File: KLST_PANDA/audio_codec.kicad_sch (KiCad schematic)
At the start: 45 parts, among them J16 MIC_IN, J17 LINE_IN, J18 HEADPHONE_OUT, J19 LINE_OUT, U9 WM8904CGEFL/V

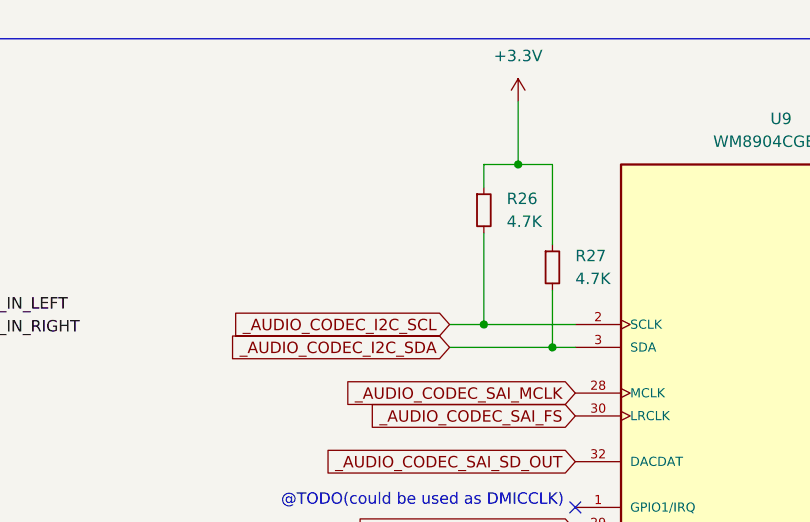
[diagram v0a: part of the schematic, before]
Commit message: changed I2C label, display can now be switched on and off
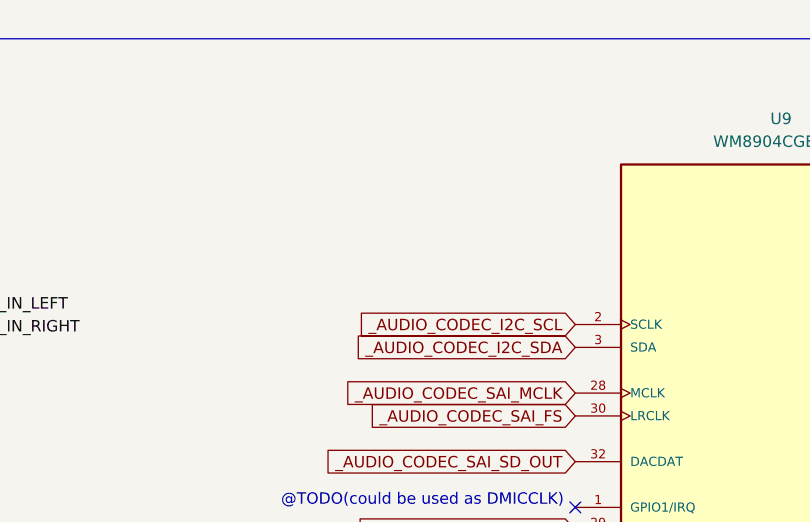
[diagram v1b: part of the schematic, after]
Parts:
- removed R26, R27: 4.7K, symbol Device:R_Small
- U9: footprint QFN40P400X400X80-33N -> WM8904CGEFL:QFN40P400X400X80-33N

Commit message: cleaned up
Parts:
- J18: value HEADPHONE_OUT -> HEADPHONE_OUT+MIC
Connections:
- net HEADPHONE_GND: no longer J18.S
- net MIC_IN_MONO: now reaches C16.2, FB1.1, J16.T
- net MIC_IN_MONO: now also J18.S
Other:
- note removed: "@TODO( consider merging microphone+headphone into a single CTIA/AHJ connector )"
- note removed: "@TODO(could be used as DMICCLK)"
- note removed: "@TODO(could be used as DMICDAT)"
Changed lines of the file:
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@@
   (junction (at 280.035 35.56) (diameter 0) (color 0 0 0 0)
   )
-  (junction (at 351.79 54.61) (diameter 0) (color 0 0 0 0)
-  )
-  (junction (at 331.47 54.61) (diameter 0) (color 0 0 0 0)
+  (junction (at 331.47 49.53) (diameter 0) (color 0 0 0 0)
   )
   (junction (at 82.55 41.91) (diameter 0) (color 0 0 0 0)
@@
   (junction (at 291.465 35.56) (diameter 0) (color 0 0 0 0)
   )
-  (junction (at 344.17 52.07) (diameter 0) (color 0 0 0 0)
+  (junction (at 344.17 46.99) (diameter 0) (color 0 0 0 0)
   )
   (junction (at 115.57 107.95) (diameter 0) (color 0 0 0 0)
@@
   )
   (junction (at 331.47 95.25) (diameter 0) (color 0 0 0 0)
+  )
+  (junction (at 50.165 44.45) (diameter 0) (color 0 0 0 0)
   )
   (junction (at 254.635 35.56) (diameter 0) (color 0 0 0 0)
@@
     (stroke (width 0) (type default))
   )
-  (wire (pts (xy 289.56 57.15) (xy 351.79 57.15))
+  (wire (pts (xy 289.56 52.07) (xy 356.87 52.07))
     (stroke (width 0) (type default))
   )
@@
     (stroke (width 0) (type default))
   )
-  (wire (pts (xy 349.25 49.53) (xy 356.87 49.53))
+  (wire (pts (xy 331.47 49.53) (xy 356.87 49.53))
     (stroke (width 0) (type default))
   )
@@
     (stroke (width 0) (type default))
   )
-  (wire (pts (xy 351.79 52.07) (xy 351.79 54.61))
-    (stroke (width 0) (type default))
-  )
   (wire (pts (xy 281.94 95.25) (xy 281.94 72.39))
     (stroke (width 0) (type default))
@@
     (stroke (width 0) (type default))
   )
-  (wire (pts (xy 331.47 54.61) (xy 331.47 78.74))
+  (wire (pts (xy 331.47 49.53) (xy 331.47 78.74))
     (stroke (width 0) (type default))
   )
@@
     (stroke (width 0) (type default))
   )
-  (wire (pts (xy 346.71 44.45) (xy 346.71 52.07))
+  (wire (pts (xy 346.71 44.45) (xy 346.71 46.99))
     (stroke (width 0) (type default))
   )
@@
     (stroke (width 0) (type default))
   )
-  (wire (pts (xy 351.79 57.15) (xy 351.79 54.61))
-    (stroke (width 0) (type default))
-  )
   (wire (pts (xy 99.06 101.6) (xy 97.79 101.6))
     (stroke (width 0) (type default))
@@
     (stroke (width 0) (type default))
   )
+  (wire (pts (xy 289.56 54.61) (xy 356.87 54.61))
+    (stroke (width 0) (type default))
+  )
   (wire (pts (xy 217.17 74.93) (xy 269.24 74.93))
     (stroke (width 0) (type default))
@@
     (stroke (width 0) (type default))
   )
-  (polyline (pts (xy 15.24 116.84) (xy 388.62 116.84))
-    (stroke (width 0) (type default))
-  )
   (wire (pts (xy 105.41 93.98) (xy 105.41 101.6))
     (stroke (width 0) (type default))
@@
     (stroke (width 0) (type default))
   )
-  (wire (pts (xy 344.17 52.07) (xy 344.17 78.74))
-    (stroke (width 0) (type default))
-  )
   (wire (pts (xy 127 87.63) (xy 121.92 87.63))
     (stroke (width 0) (type default))
@@
     (stroke (width 0) (type default))
   )
-  (wire (pts (xy 331.47 54.61) (xy 349.25 54.61))
-    (stroke (width 0) (type default))
-  )
-  (wire (pts (xy 38.1 44.45) (xy 60.96 44.45))
+  (wire (pts (xy 38.1 44.45) (xy 50.165 44.45))
     (stroke (width 0) (type default))
   )
@@
     (stroke (width 0) (type default))
   )
+  (wire (pts (xy 50.165 44.45) (xy 60.96 44.45))
+    (stroke (width 0) (type default))
+  )
   (wire (pts (xy 105.41 83.82) (xy 104.14 83.82))
     (stroke (width 0) (type default))
@@
     (stroke (width 0) (type default))
   )
-  (wire (pts (xy 344.17 52.07) (xy 346.71 52.07))
+  (wire (pts (xy 344.17 46.99) (xy 346.71 46.99))
     (stroke (width 0) (type default))
   )
@@
     (stroke (width 0) (type default))
   )
-  (wire (pts (xy 351.79 54.61) (xy 356.87 54.61))
-    (stroke (width 0) (type default))
-  )
   (wire (pts (xy 38.1 91.44) (xy 46.99 91.44))
     (stroke (width 0) (type default))
@@
     (stroke (width 0) (type default))
   )
-  (wire (pts (xy 349.25 49.53) (xy 349.25 54.61))
-    (stroke (width 0) (type default))
-  )
   (wire (pts (xy 289.56 62.23) (xy 318.77 62.23))
     (stroke (width 0) (type default))
@@
     (stroke (width 0) (type default))
   )
+  (wire (pts (xy 344.17 46.99) (xy 344.17 78.74))
+    (stroke (width 0) (type default))
+  )
   (wire (pts (xy 99.06 48.26) (xy 99.06 52.07))
     (stroke (width 0) (type default))
@@
     (stroke (width 0) (type default))
   )
-  (wire (pts (xy 289.56 54.61) (xy 331.47 54.61))
+  (wire (pts (xy 289.56 49.53) (xy 331.47 49.53))
     (stroke (width 0) (type default))
   )
@@
     (stroke (width 0) (type default))
   )
-  (polyline (pts (xy 15.24 116.84) (xy 15.24 15.24))
-    (stroke (width 0) (type default))
-  )
   (wire (pts (xy 220.98 22.225) (xy 220.98 31.75))
     (stroke (width 0) (type default))
   )
-  (wire (pts (xy 351.79 52.07) (xy 356.87 52.07))
+  (wire (pts (xy 50.165 26.67) (xy 50.165 44.45))
     (stroke (width 0) (type default))
   )
@@
     (stroke (width 0) (type default))
   )
-  (wire (pts (xy 289.56 52.07) (xy 344.17 52.07))
+  (wire (pts (xy 289.56 46.99) (xy 344.17 46.99))
     (stroke (width 0) (type default))
   )
@@
     (stroke (width 0) (type default))
   )
-  (polyline (pts (xy 388.62 15.24) (xy 388.62 116.84))
-    (stroke (width 0) (type default))
-  )
   (wire (pts (xy 86.36 107.95) (xy 115.57 107.95))
     (stroke (width 0) (type default))
@@
     (stroke (width 0) (type default))
   )
-  (polyline (pts (xy 15.24 15.24) (xy 388.62 15.24))
-    (stroke (width 0) (type default))
-  )
   (wire (pts (xy 254.635 22.225) (xy 254.635 25.4))
     (stroke (width 0) (type default))
@@
     (stroke (width 0) (type default))
   )
+  (rectangle (start 15.24 15.24) (end 396.24 119.38)
+    (stroke (width 0) (type default))
+    (fill (type none))
+  )
   (rectangle (start 250.825 24.13) (end 314.325 36.83)
     (stroke (width 0) (type default))
     (fill (type none))
+  )
+  (text_box "MIC_IN_MONO is connected to MIC_IN_LEFT and SLEEVE ( CTIA/AHJ )"
+    (at 360.68 27.305 0) (size 24.13 10.16)
+    (stroke (width 0) (type default))
+    (fill (type none))
+    (effects (font (size 1.27 1.27)) (justify left bottom))
   )
   (text "see datasheet Table 95, p177" (at 227.33 105.41 0)
@@
     (effects (font (size 1.27 1.27)) (justify left bottom))
   )
-  (text "@TODO(could be used as DMICDAT)" (at 157.48 74.93 0)
-    (effects (font (size 1.27 1.27)) (justify right bottom))
-  )
-  (text "@TODO( consider merging microphone+headphone into a single CTIA/AHJ connector )"
-    (at 332.74 43.18 0)
-    (effects (font (size 1.27 1.27)) (justify left bottom))
-  )
   (text "TANTALUM" (at 97.79 106.68 0)
     (effects (font (size 1.27 1.27)) (justify left bottom))
@@
   (text "6.3V" (at 246.38 101.6 0)
     (effects (font (size 1.27 1.27)) (justify left bottom))
-  )
-  (text "@TODO(could be used as DMICCLK)" (at 170.18 67.31 0)
-    (effects (font (size 1.27 1.27)) (justify right bottom))
   )
   (text "should be reasonably close to WM8904" (at 302.26 77.47 0)
@@
     (effects (font (size 1.27 1.27)) (justify right bottom))
   )
+  (label "MIC_IN_MONO" (at 289.56 54.61 0) (fields_autoplaced)
+    (effects (font (size 1.27 1.27)) (justify left bottom))
+  )
   (label "LINE_IN_LEFT" (at 171.45 82.55 180) (fields_autoplaced)
     (effects (font (size 1.27 1.27)) (justify right bottom))
   )
-  (label "HEADPHONE_GND" (at 289.56 57.15 0) (fields_autoplaced)
+  (label "HEADPHONE_GND" (at 289.56 52.07 0) (fields_autoplaced)
     (effects (font (size 1.27 1.27)) (justify left bottom))
   )
@@
     (effects (font (size 1.27 1.27)) (justify left bottom))
   )
-  (label "HEADPHONE_LEFT" (at 289.56 52.07 0) (fields_autoplaced)
+  (label "HEADPHONE_LEFT" (at 289.56 46.99 0) (fields_autoplaced)
     (effects (font (size 1.27 1.27)) (justify left bottom))
   )
@@
     (effects (font (size 1.27 1.27)) (justify left bottom))
   )
+  (label "MIC_IN_MONO" (at 50.165 26.67 0) (fields_autoplaced)
+    (effects (font (size 1.27 1.27)) (justify left bottom))
+  )
   (label "MIC_IN_LEFT" (at 104.14 45.72 0) (fields_autoplaced)
     (effects (font (size 1.27 1.27)) (justify left bottom))
@@
     (effects (font (size 1.27 1.27)) (justify left bottom))
   )
-  (label "HEADPHONE_RIGHT" (at 289.56 54.61 0) (fields_autoplaced)
+  (label "HEADPHONE_RIGHT" (at 289.56 49.53 0) (fields_autoplaced)
     (effects (font (size 1.27 1.27)) (justify left bottom))
   )
@@
       (effects (font (size 1.27 1.27)) (justify right))
     )
-    (property "Value" "HEADPHONE_OUT" (at 370.84 49.53 0)
+    (property "Value" "HEADPHONE_OUT+MIC" (at 370.84 49.53 0)
       (effects (font (size 1.27 1.27)) (justify right))
     )

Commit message: removed GDNA
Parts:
- renumbered U9 to U10
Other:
- note removed: "@TODO(maybe better connect AGND to VSSA?!?)"
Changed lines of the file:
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@@
-    (effects (font (size 1.27 1.27)) (justify left bottom))
-  )
-  (text "@TODO(maybe better connect AGND to VSSA?!?)" (at 177.8 113.665 0)
     (effects (font (size 1.27 1.27)) (justify left bottom))
   )
@@
         )
         (path "/b4513875-4c57-4720-bcc5-43ead67fe18f/88042be3-8ae4-47d6-9c31-0a9af833bdb2"
-          (reference "R79") (unit 1)
+          (reference "R81") (unit 1)
         )
       )
@@
         )
         (path "/b4513875-4c57-4720-bcc5-43ead67fe18f/88042be3-8ae4-47d6-9c31-0a9af833bdb2"
-          (reference "#PWR099") (unit 1)
+          (reference "#PWR097") (unit 1)
         )
       )
@@
         )
         (path "/b4513875-4c57-4720-bcc5-43ead67fe18f/88042be3-8ae4-47d6-9c31-0a9af833bdb2"
-          (reference "R73") (unit 1)
+          (reference "R75") (unit 1)
         )
       )
@@
   (symbol (lib_id "power:+3.3V") (at 220.98 22.225 0) (unit 1)
     (in_bom yes) (on_board yes) (dnp no) (fields_autoplaced)
-    (property "Reference" "#PWR096" (at 220.98 26.035 0)
+    (property "Reference" "#PWR094" (at 220.98 26.035 0)
       (effects (font (size 1.27 1.27)) hide)
     )
@@
       (project "KLST_PANDA"
         (path "/b4513875-4c57-4720-bcc5-43ead67fe18f/88042be3-8ae4-47d6-9c31-0a9af833bdb2"
-          (reference "#PWR096") (unit 1)
+          (reference "#PWR094") (unit 1)
         )
       )
@@
         )
         (path "/b4513875-4c57-4720-bcc5-43ead67fe18f/88042be3-8ae4-47d6-9c31-0a9af833bdb2"
-          (reference "R77") (unit 1)
+          (reference "R79") (unit 1)
         )
       )
@@
         )
         (path "/b4513875-4c57-4720-bcc5-43ead67fe18f/88042be3-8ae4-47d6-9c31-0a9af833bdb2"
-          (reference "#PWR094") (unit 1)
+          (reference "#PWR092") (unit 1)
         )
       )
@@
         )
         (path "/b4513875-4c57-4720-bcc5-43ead67fe18f/88042be3-8ae4-47d6-9c31-0a9af833bdb2"
-          (reference "R78") (unit 1)
+          (reference "R80") (unit 1)
         )
       )
@@
         )
         (path "/b4513875-4c57-4720-bcc5-43ead67fe18f/88042be3-8ae4-47d6-9c31-0a9af833bdb2"
-          (reference "#PWR0100") (unit 1)
+          (reference "#PWR098") (unit 1)
         )
       )
@@
         )
         (path "/b4513875-4c57-4720-bcc5-43ead67fe18f/88042be3-8ae4-47d6-9c31-0a9af833bdb2"
-          (reference "R71") (unit 1)
+          (reference "R73") (unit 1)
         )
       )
@@
         )
         (path "/b4513875-4c57-4720-bcc5-43ead67fe18f/88042be3-8ae4-47d6-9c31-0a9af833bdb2"
-          (reference "R69") (unit 1)
+          (reference "R71") (unit 1)
         )
       )
@@
         )
         (path "/b4513875-4c57-4720-bcc5-43ead67fe18f/88042be3-8ae4-47d6-9c31-0a9af833bdb2"
-          (reference "R75") (unit 1)
+          (reference "R77") (unit 1)
         )
       )
@@
         )
         (path "/b4513875-4c57-4720-bcc5-43ead67fe18f/88042be3-8ae4-47d6-9c31-0a9af833bdb2"
-          (reference "#PWR095") (unit 1)
+          (reference "#PWR093") (unit 1)
         )
       )
@@
         )
         (path "/b4513875-4c57-4720-bcc5-43ead67fe18f/88042be3-8ae4-47d6-9c31-0a9af833bdb2"
-          (reference "R72") (unit 1)
+          (reference "R74") (unit 1)
         )
       )
@@
   (symbol (lib_id "power:+3.3V") (at 254.635 22.225 0) (unit 1)
     (in_bom yes) (on_board yes) (dnp no) (fields_autoplaced)
-    (property "Reference" "#PWR097" (at 254.635 26.035 0)
+    (property "Reference" "#PWR095" (at 254.635 26.035 0)
       (effects (font (size 1.27 1.27)) hide)
     )
@@
       (project "KLST_PANDA"
         (path "/b4513875-4c57-4720-bcc5-43ead67fe18f/88042be3-8ae4-47d6-9c31-0a9af833bdb2"
-          (reference "#PWR097") (unit 1)
+          (reference "#PWR095") (unit 1)
         )
       )
@@
         )
         (path "/b4513875-4c57-4720-bcc5-43ead67fe18f/88042be3-8ae4-47d6-9c31-0a9af833bdb2"
-          (reference "R74") (unit 1)
+          (reference "R76") (unit 1)
         )
       )
@@
   (symbol (lib_id "WM8904CGEFL:WM8904CGEFL/V") (at 194.31 64.77 0) (unit 1)
     (in_bom yes) (on_board yes) (dnp no) (fields_autoplaced)
-    (property "Reference" "U9" (at 194.31 24.13 0)
+    (property "Reference" "U10" (at 194.31 24.13 0)
       (effects (font (size 1.27 1.27)))
     )
@@
       (project "KLST_PANDA"
         (path "/b4513875-4c57-4720-bcc5-43ead67fe18f/88042be3-8ae4-47d6-9c31-0a9af833bdb2"
-          (reference "U9") (unit 1)
+          (reference "U10") (unit 1)
         )
       )
@@
         )
         (path "/b4513875-4c57-4720-bcc5-43ead67fe18f/88042be3-8ae4-47d6-9c31-0a9af833bdb2"
-          (reference "R70") (unit 1)
+          (reference "R72") (unit 1)
         )
       )
@@
         )
         (path "/b4513875-4c57-4720-bcc5-43ead67fe18f/88042be3-8ae4-47d6-9c31-0a9af833bdb2"
-          (reference "R80") (unit 1)
+          (reference "R82") (unit 1)
         )
       )
@@
         )
         (path "/b4513875-4c57-4720-bcc5-43ead67fe18f/88042be3-8ae4-47d6-9c31-0a9af833bdb2"
-          (reference "#PWR098") (unit 1)
+          (reference "#PWR096") (unit 1)
         )
       )
@@
         )
         (path "/b4513875-4c57-4720-bcc5-43ead67fe18f/88042be3-8ae4-47d6-9c31-0a9af833bdb2"
-          (reference "R76") (unit 1)
-        )
-      )
+          (reference "R78") (unit 1)
+        )
+      )

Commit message: resolved TODOs
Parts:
- renumbered U10 to U12
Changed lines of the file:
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@@
   (symbol (lib_id "WM8904CGEFL:WM8904CGEFL/V") (at 194.31 64.77 0) (unit 1)
     (in_bom yes) (on_board yes) (dnp no) (fields_autoplaced)
-    (property "Reference" "U10" (at 194.31 24.13 0)
+    (property "Reference" "U12" (at 194.31 24.13 0)
       (effects (font (size 1.27 1.27)))
     )
@@
       (project "KLST_PANDA"
         (path "/b4513875-4c57-4720-bcc5-43ead67fe18f/88042be3-8ae4-47d6-9c31-0a9af833bdb2"
-          (reference "U10") (unit 1)
+          (reference "U12") (unit 1)
         )
       )

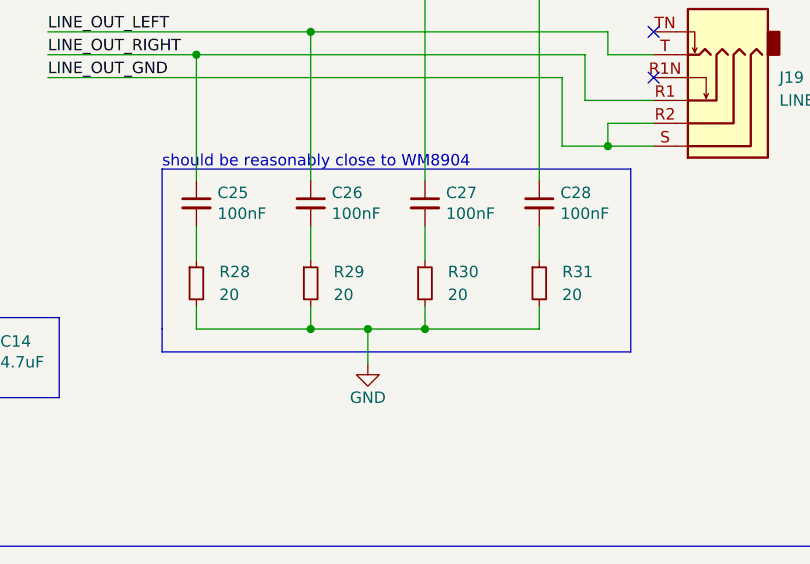
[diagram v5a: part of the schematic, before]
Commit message: started spec'ing components
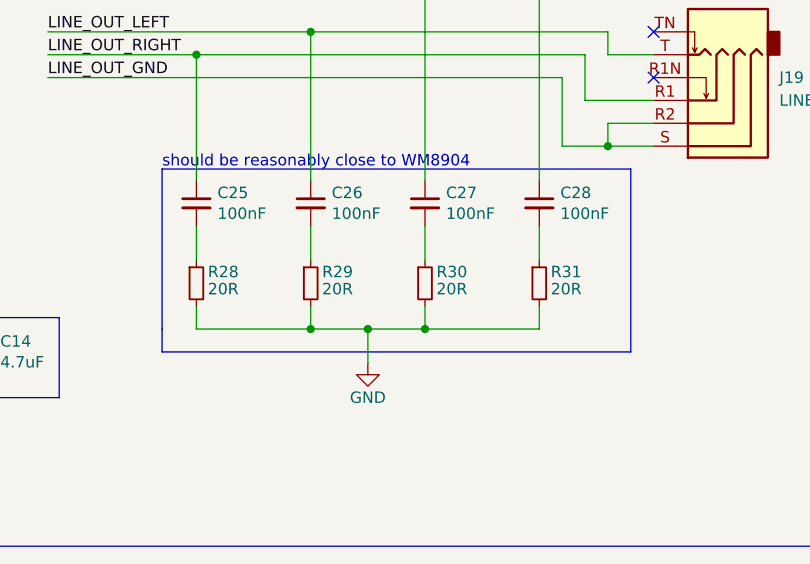
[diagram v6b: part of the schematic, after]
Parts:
- C10, C8: JLCPCB (none) -> C12530
- C11, C13, C25, C26, C27, C28, C5, C7, C9: JLCPCB (none) -> C1525; LCSC C1525 -> (none)
- C12, C14: JLCPCB (none) -> C23733
- C15, C18: footprint (none) -> Capacitor_SMD:C_0402_1005Metric; JLCPCB (none) -> C1530
- C16, C17: footprint (none) -> Capacitor_SMD:C_0402_1005Metric; JLCPCB (none) -> C1537
- C19, C20, C22, C23: footprint (none) -> Capacitor_SMD:C_0402_1005Metric; JLCPCB (none) -> C52923
- C21, C24: footprint (none) -> Capacitor_Tantalum_SMD:CP_EIA-3216-18_Kemet-A; JLCPCB (none) -> C7171
- C6: footprint Capacitor_SMD:C_0603_1608Metric -> Capacitor_SMD:C_0402_1005Metric; JLCPCB (none) -> C107370
- FB1, FB2: footprint (none) -> Inductor_SMD:L_0402_1005Metric; JLCPCB (none) -> C160969; LCSC C160969 -> (none)
- J16, J17, J18, J19: JLCPCB (none) -> C128987; JLCPCB Part # C128987 -> (none)
- R24, R25: footprint (none) -> Resistor_SMD:R_0805_2012Metric_Pad1.20x1.40mm_HandSolder; JLCPCB (none) -> C103914
- R28, R29, R30, R31: value 20 -> 20R
